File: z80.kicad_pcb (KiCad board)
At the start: 2 copper layers, 144.8 x 172.7 mm, 93 parts, among them J1 Conn_02x08_Odd_Even, J2 KMDGX-6S-BS, J3 Conn_02x20_Odd_Even, J5 USB_B, J6 PWR, SW1 KS01Q, U1 Z80CPU, U10 Z84C40, U11 SP232E, U12 SP232E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

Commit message: Initial prototype PCB build.
git-svn-id: svn+ssh://dev.thehead.ca/depot/main/z80@619 995eaefb-0ce2-40e3-b8bc-69bf8729875b
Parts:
- added REF**: MountingHole_3.2mm_M3_Pad, Mounting_Holes:MountingHole_3.2mm_M3_Pad, F.Cu at (20.0, 20.0)
- added REF**: MountingHole_3.2mm_M3_Pad, Mounting_Holes:MountingHole_3.2mm_M3_Pad, F.Cu at (20.0, 179.0)
- added REF**: MountingHole_3.2mm_M3_Pad, Mounting_Holes:MountingHole_3.2mm_M3_Pad, F.Cu at (155.0, 179.0)
- added REF**: MountingHole_3.2mm_M3_Pad, Mounting_Holes:MountingHole_3.2mm_M3_Pad, F.Cu at (155.0, 20.0)
- moved R3 37.5 mm to (114.8, 153.3), turned to 180 degrees
- moved R2 36.5 mm to (67.9, 159.2), turned to 180 degrees
- moved R5 34.1 mm to (114.8, 156.0), turned to 180 degrees
- moved R4 33.4 mm to (67.9, 161.9), turned to 180 degrees
- moved R7 30.7 mm to (114.8, 158.6), turned to 180 degrees
- moved R6 30.3 mm to (67.9, 164.5), turned to 180 degrees
- moved R8 27.4 mm to (67.9, 167.2), turned to 180 degrees
- moved R9 27.4 mm to (114.8, 161.3), turned to 180 degrees
- moved R10 24.7 mm to (67.9, 169.8), turned to 180 degrees
- moved R11 24.2 mm to (114.8, 163.8), turned to 180 degrees
- moved JOY1 6.11 mm to (38.4, 171.1)
- moved JOY2 5.41 mm to (83.7, 171.1)
- moved J5 5.40 mm to (31.2, 30.0)
- moved J2 4.51 mm to (51.5, 15.0)
- moved C18 4.14 mm to (103.4, 38.1)
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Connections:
- J3 pad 28: (no net) -> /~IORQ7
- J3 pad 30: (no net) -> /~IORQ5
- J3 pad 32: (no net) -> /~IORQ6
- U6 pad 10: (no net) -> /~IORQ5
- U6 pad 7: (no net) -> /~IORQ7
- U6 pad 9: (no net) -> /~IORQ6
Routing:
- net GND: track 786.4 -> 617.9 mm
- net Net-(JOY1-Pad1): track 15.0 -> 43.8 mm
- net Net-(JOY2-Pad1): track 15.0 -> 43.0 mm
- net Net-(JOY1-Pad2): track 15.1 -> 42.1 mm
- net Net-(JOY1-Pad3): track 15.2 -> 40.4 mm
- net Net-(JOY2-Pad2): track 15.1 -> 39.1 mm
- net Net-(JOY1-Pad4): track 15.3 -> 38.4 mm
- net Net-(JOY2-Pad3): track 15.2 -> 35.6 mm
- net /~IORQ6: track 0.00 -> 19.6 mm
- net /~IORQ5: track 0.00 -> 19.6 mm
- net Net-(JOY2-Pad4): track 15.3 -> 33.7 mm
- net Net-(JOY1-Pad6): track 24.7 -> 40.5 mm
- net Net-(JOY2-Pad6): track 24.6 -> 39.5 mm
- net VCC: track 618.0 -> 605.4 mm
- net /~IORQ7: track 0.00 -> 11.0 mm
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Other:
- board size 144.8 x 172.7 mm -> 145 x 169 mm
- board text added: "Z80 Prototype rev 8 2018/05/30 dan.collens@gmail.com"

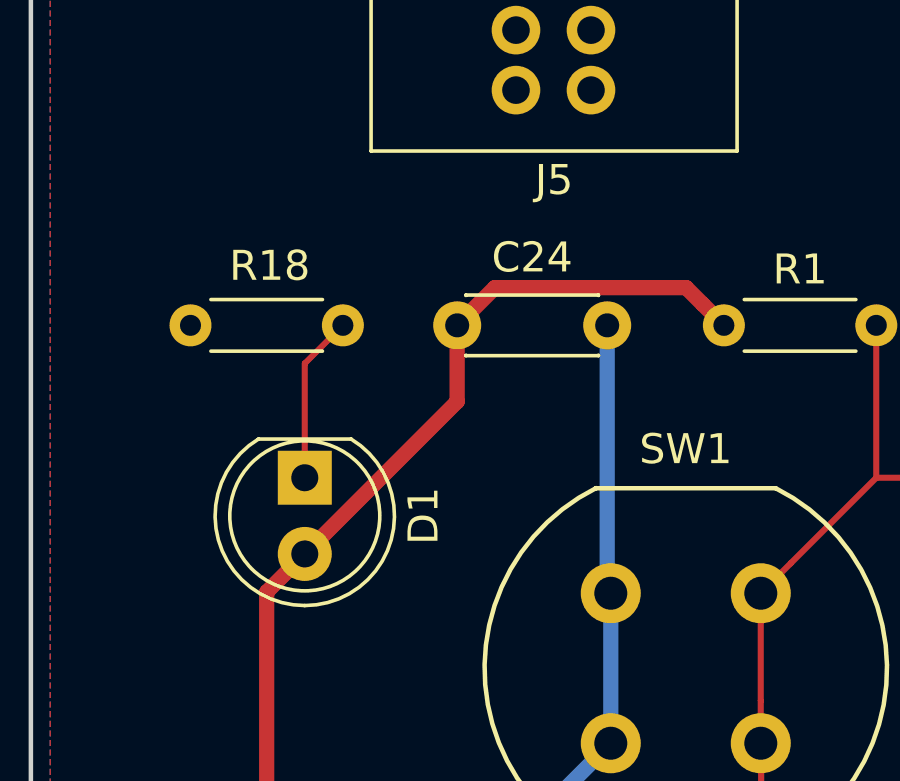
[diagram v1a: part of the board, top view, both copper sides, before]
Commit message: Fix footprint for C24 to be a polarized radial electrolytic THT capacitor.
git-svn-id: svn+ssh://dev.thehead.ca/depot/main/z80@621 995eaefb-0ce2-40e3-b8bc-69bf8729875b
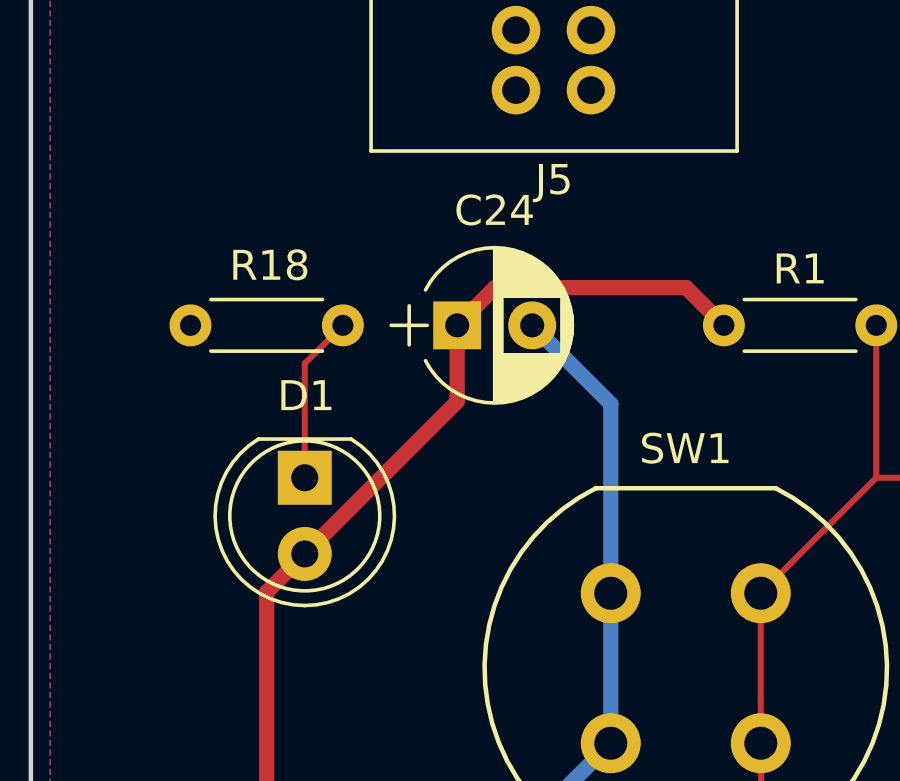
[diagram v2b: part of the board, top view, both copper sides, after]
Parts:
- C24: footprint Capacitors_THT:C_Disc_D4.3mm_W1.9mm_P5.00mm -> Capacitors_THT:CP_Radial_D5.0mm_P2.50mm
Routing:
- net GND: track 617.9 -> 619.0 mm

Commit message: Update schematic & layout to fix reversed keyboard port pinout. Update test programs for PCB. Write test code for joystick port.
git-svn-id: svn+ssh://dev.thehead.ca/depot/main/z80@622 995eaefb-0ce2-40e3-b8bc-69bf8729875b
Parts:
- moved R30 10.5 mm to (48.0, 35.8)
- moved R31 0.79 mm to (55.3, 35.8), turned to 90 degrees
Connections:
- J2 pad 1: (no net) -> Net-(J2-Pad1)
- J2 pad 2: Net-(J2-Pad2) -> (no net)
- J2 pad 3: VCC -> GND
- J2 pad 5: GND -> VCC
- J2 pad 6: (no net) -> /PIO/KCLK
- J2 pad 8: /PIO/KCLK -> (no net)
- R31 pad 2: Net-(J2-Pad2) -> Net-(J2-Pad1)
- U2 pad 11: Net-(J2-Pad2) -> Net-(J2-Pad1)
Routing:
- net Net-(J2-Pad1): track 0.00 -> 31.8 mm
- net Net-(J2-Pad2): track 30.5 -> 0.00 mm
- net VCC: track 605.4 -> 594.7 mm
- net /PIO/KCLK: track 163.8 -> 167.7 mm
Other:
- board text added: "Z80 Prototype rev 10 2018/06/12 dan.collens@gmail.com"
- board text removed: "Z80 Prototype rev 8 2018/05/30 dan.collens@gmail.com"
